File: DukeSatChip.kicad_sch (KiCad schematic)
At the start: 13 parts, among them J1 Conn_01x02_Pin, Q1 AO3401A

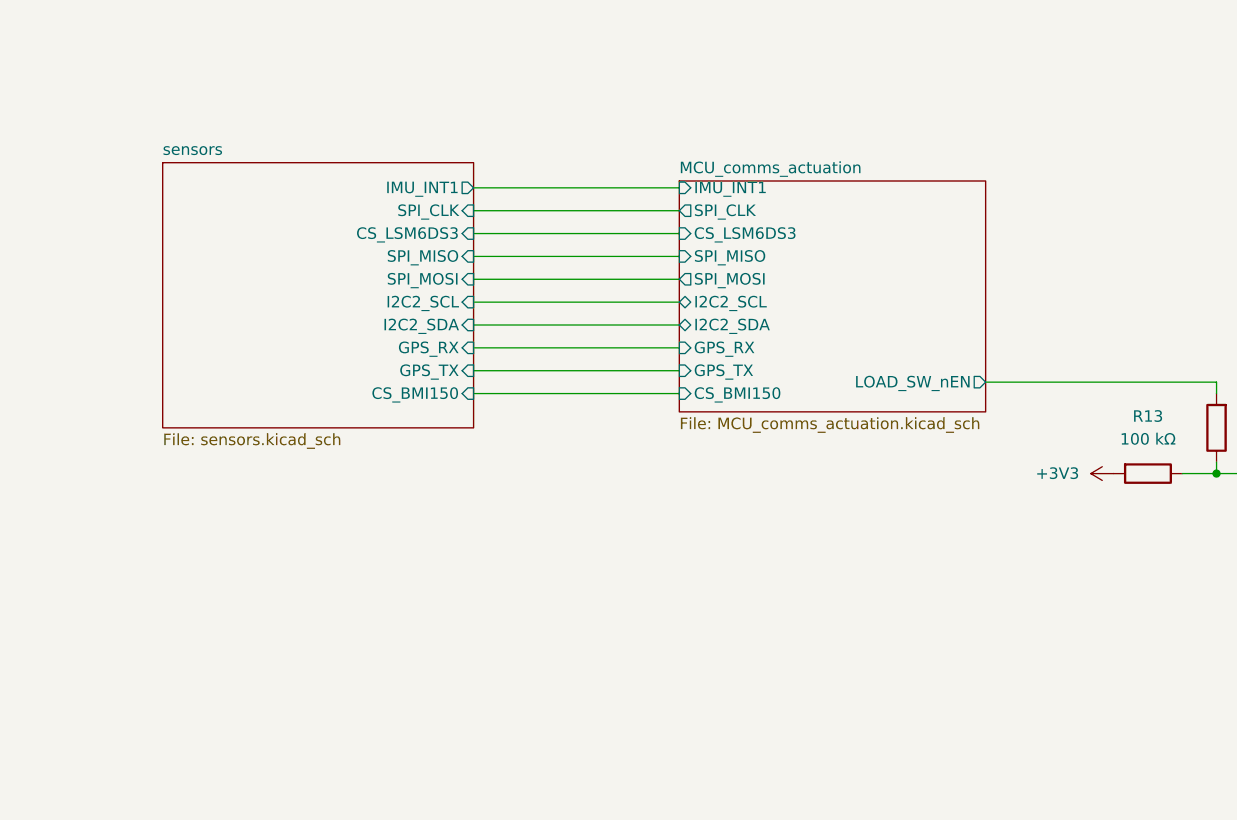
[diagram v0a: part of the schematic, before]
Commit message: Add XYZ photodiodes to sun sensor. Fix hierarchical labels on MCU.
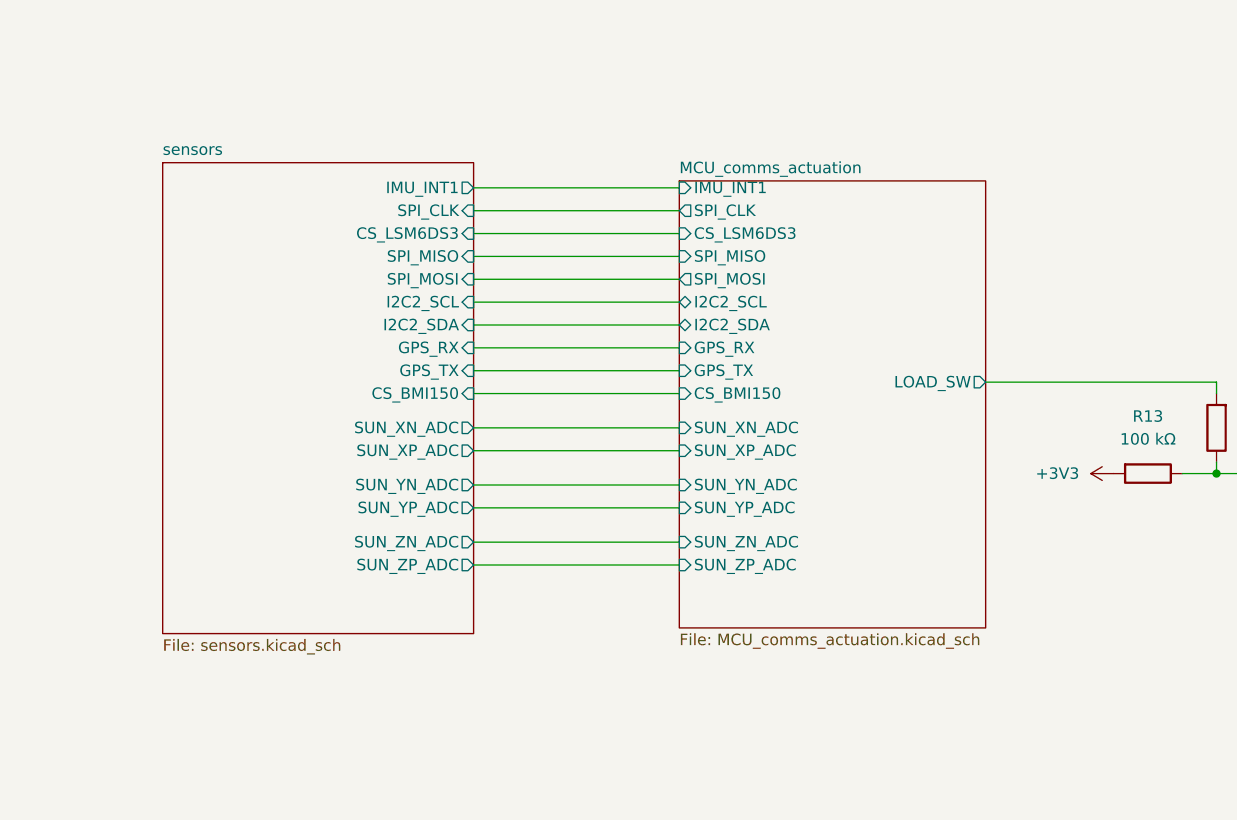
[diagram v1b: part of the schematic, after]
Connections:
- net MCU_comms_actuation/LOAD_SW_nEN renamed MCU_comms_actuation/LOAD_SW
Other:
- sheet MCU_comms_actuation ports: added LOAD_SW, SUN_XN_ADC, SUN_XP_ADC, SUN_YN_ADC, SUN_YP_ADC, SUN_ZN_ADC, SUN_ZP_ADC; removed LOAD_SW_nEN
- sheet sensors ports: added SUN_XN_ADC, SUN_XP_ADC, SUN_YN_ADC, SUN_YP_ADC, SUN_ZN_ADC, SUN_ZP_ADC; removed none
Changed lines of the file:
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@@
 	(wire
 		(pts
+			(xy 167.64 100.33) (xy 190.5 100.33)
+		)
+		(stroke
+			(width 0)
+			(type default)
+		)
+	)
+	(wire
+		(pts
 			(xy 96.52 50.8) (xy 104.14 50.8)
 		)
@@
 	(wire
 		(pts
+			(xy 167.64 106.68) (xy 190.5 106.68)
+		)
+		(stroke
+			(width 0)
+			(type default)
+		)
+	)
+	(wire
+		(pts
 			(xy 167.64 83.82) (xy 190.5 83.82)
 		)
@@
 	(wire
 		(pts
+			(xy 167.64 104.14) (xy 190.5 104.14)
+		)
+		(stroke
+			(width 0)
+			(type default)
+		)
+	)
+	(wire
+		(pts
 			(xy 69.85 58.42) (xy 67.31 58.42)
 		)
@@
 	(wire
 		(pts
+			(xy 167.64 97.79) (xy 190.5 97.79)
+		)
+		(stroke
+			(width 0)
+			(type default)
+		)
+	)
+	(wire
+		(pts
 			(xy 167.64 86.36) (xy 190.5 86.36)
 		)
@@
 	(wire
 		(pts
+			(xy 167.64 110.49) (xy 190.5 110.49)
+		)
+		(stroke
+			(width 0)
+			(type default)
+		)
+	)
+	(wire
+		(pts
 			(xy 167.64 78.74) (xy 190.5 78.74)
 		)
@@
 		)
 	)
+	(wire
+		(pts
+			(xy 167.64 113.03) (xy 190.5 113.03)
+		)
+		(stroke
+			(width 0)
+			(type default)
+		)
+	)
 	(image
 		(at 397.51 260.35)
@@
 	(sheet
 		(at 190.5 70.358)
-		(size 34.036 25.654)
+		(size 34.036 49.657)
 		(exclude_from_sim no)
 		(in_bom yes)
@@
 		)
 		(property "Sheetfile" "MCU_comms_actuation.kicad_sch"
-			(at 190.5 96.5966 0)
+			(at 190.5 120.5996 0)
 			(show_name no)
 			(do_not_autoplace no)
@@
 			)
 		)
-		(pin "LOAD_SW_nEN" output
+		(pin "LOAD_SW" output
 			(at 224.536 92.71 0)
 			(effects
@@
 			)
 		)
+		(pin "SUN_XN_ADC" input
+			(at 190.5 97.79 180)
+			(effects
+				(font
+					(size 1.27 1.27)
+				)
+				(justify left)
+			)
+		)
+		(pin "SUN_XP_ADC" input
+			(at 190.5 100.33 180)
+			(effects
+				(font
+					(size 1.27 1.27)
+				)
+				(justify left)
+			)
+		)
+		(pin "SUN_YN_ADC" input
+			(at 190.5 104.14 180)
+			(effects
+				(font
+					(size 1.27 1.27)
+				)
+				(justify left)
+			)
+		)
+		(pin "SUN_YP_ADC" input
+			(at 190.5 106.68 180)
+			(effects
+				(font
+					(size 1.27 1.27)
+				)
+				(justify left)
+			)
+		)
+		(pin "SUN_ZN_ADC" input
+			(at 190.5 110.49 180)
+			(effects
+				(font
+					(size 1.27 1.27)
+				)
+				(justify left)
+			)
+		)
+		(pin "SUN_ZP_ADC" input
+			(at 190.5 113.03 180)
+			(effects
+				(font
+					(size 1.27 1.27)
+				)
+				(justify left)
+			)
+		)
 		(instances
 			(project "DukeSatChip"
@@
 	(sheet
 		(at 133.096 68.326)
-		(size 34.544 29.464)
+		(size 34.544 52.324)
 		(exclude_from_sim no)
 		(in_bom yes)
@@
 		)
 		(property "Sheetfile" "sensors.kicad_sch"
-			(at 133.096 98.3746 0)
+			(at 133.096 121.2346 0)
 			(show_name no)
 			(do_not_autoplace no)
@@
 			(effects
 				(font
+					(size 1.27 1.27)
+				)
+				(justify right)
+			)
+		)
+		(pin "SUN_XN_ADC" output
+			(at 167.64 97.79 0)
+			(effects
+				(font
+					(size 1.27 1.27)
+				)
+				(justify right)
+			)
+		)
+		(pin "SUN_XP_ADC" output
+			(at 167.64 100.33 0)
+			(effects
+				(font
+					(size 1.27 1.27)
+				)
+				(justify right)
+			)
+		)
+		(pin "SUN_YN_ADC" output
+			(at 167.64 104.14 0)
+			(effects
+				(font
+					(size 1.27 1.27)
+				)
+				(justify right)
+			)
+		)
+		(pin "SUN_YP_ADC" output
+			(at 167.64 106.68 0)
+			(effects
+				(font
+					(size 1.27 1.27)
+				)
+				(justify right)
+			)
+		)
+		(pin "SUN_ZN_ADC" output
+			(at 167.64 110.49 0)
+			(effects
+				(font
+					(size 1.27 1.27)
+				)
+				(justify right)
+			)
+		)
+		(pin "SUN_ZP_ADC" output
+			(at 167.64 113.03 0)
+			(effects
+				(font

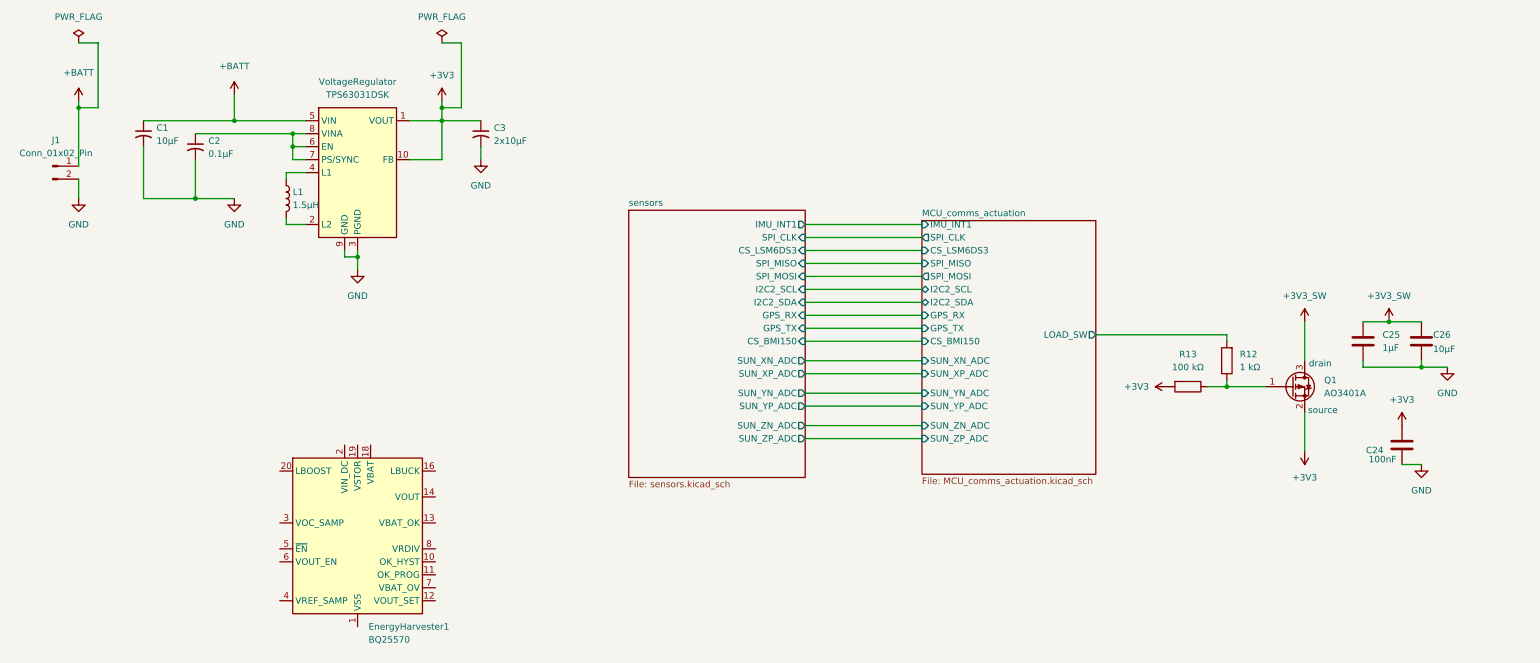
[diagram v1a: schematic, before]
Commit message: Fix sun sensor axis label mismatch
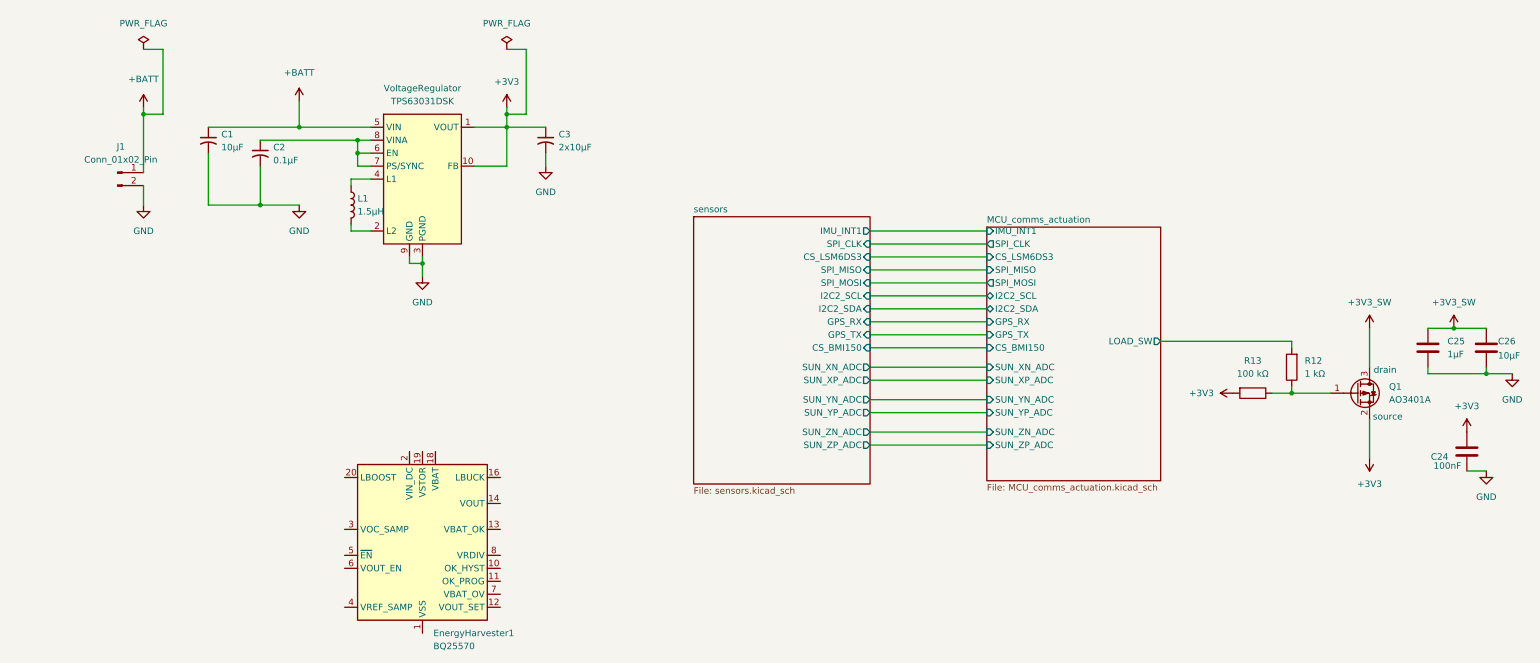
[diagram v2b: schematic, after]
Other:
- moved on the sheet: C1, C2, C24, C25, C26, C3, EnergyHarvester1, J1, L1, Q1, R12, R13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
